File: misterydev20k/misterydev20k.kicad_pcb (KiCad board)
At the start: 2 copper layers, 90 x 67 mm, 178 parts, among them J1 SWD, J11 Joystick 0, J12 Joystick 1, J13 USB_A_Stacked, J2 USB_C_Receptacle_USB2.0, J3 Jumper block, J4 Micro_SD_Card_Det1, J5 HDMI_A, J6 Grove 1125S-4P, J7 USB_A_Stacked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

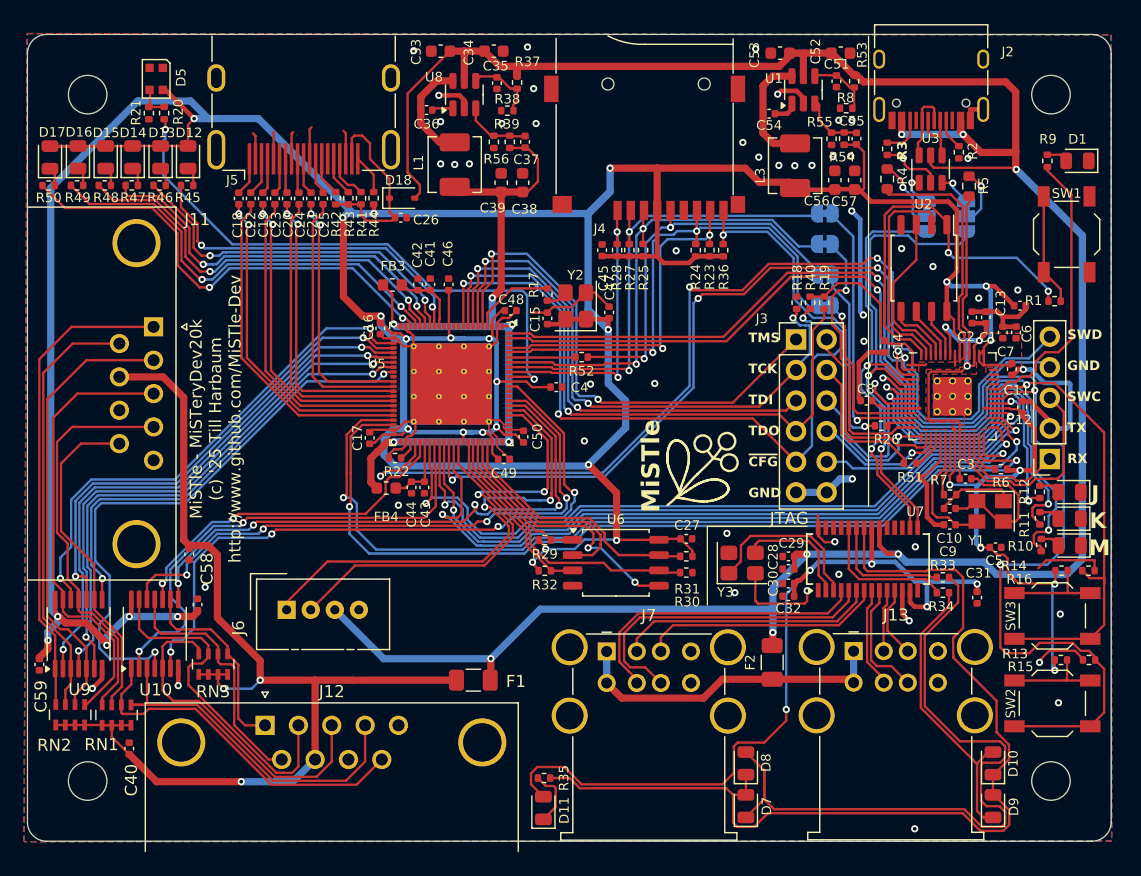
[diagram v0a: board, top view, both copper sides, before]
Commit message: Length match TMDS signals
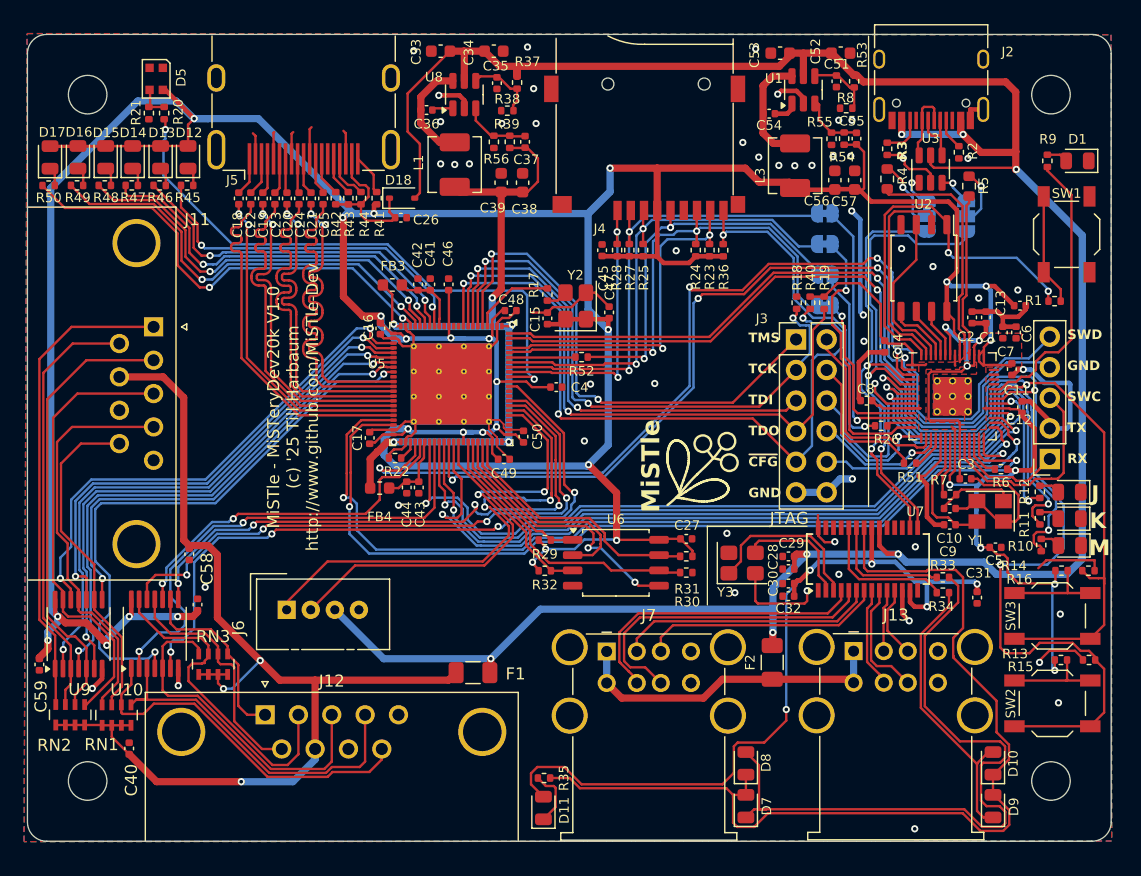
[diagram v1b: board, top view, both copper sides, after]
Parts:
- moved J12 0.87 mm to (119.7, 96.5)
- moved F1 0.63 mm to (137.0, 93.0)
- moved FB4 0.54 mm to (129.2, 77.7)
- moved C43 0.46 mm to (132.5, 77.6)
- moved C44 0.40 mm to (131.5, 77.6)
- moved R41 0.25 mm to (129.0, 53.6)
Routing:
- net +3V3: track 441.4 -> 432.4 mm
- net CK-: track 21.7 -> 29.9 mm
- net CK+: track 20.8 -> 26.9 mm
- net D0-: track 24.2 -> 30.0 mm
- net D1-: track 26.0 -> 30.1 mm
- net 5V_DVI: track 16.8 -> 12.8 mm
- net D0+: track 23.8 -> 27.0 mm
- net D2-: track 27.7 -> 30.2 mm
- net Net-(D7-K): track 60.0 -> 58.1 mm
- net D1+: track 25.4 -> 27.1 mm
- net Net-(RN3-R3.1): track 29.0 -> 27.9 mm
- net MODE0: track 113.6 -> 112.6 mm
- net Net-(RN3-R2.1): track 21.0 -> 20.0 mm
- net Net-(RN3-R1.1): track 16.4 -> 15.4 mm
- net Net-(RN1-R2.1): track 29.4 -> 30.0 mm
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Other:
- board text added: "MiSTle - MiSTeryDev20k V1.0 (c) '25 Till Harbaum http://www.github.com/MiSTle-Dev"
- board text removed: "MiSTle - MiSTeryDev20k (c) '25 Till Harbaum http://www.github.com/MiSTle-Dev"

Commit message: Dev20k LCSC part mapping
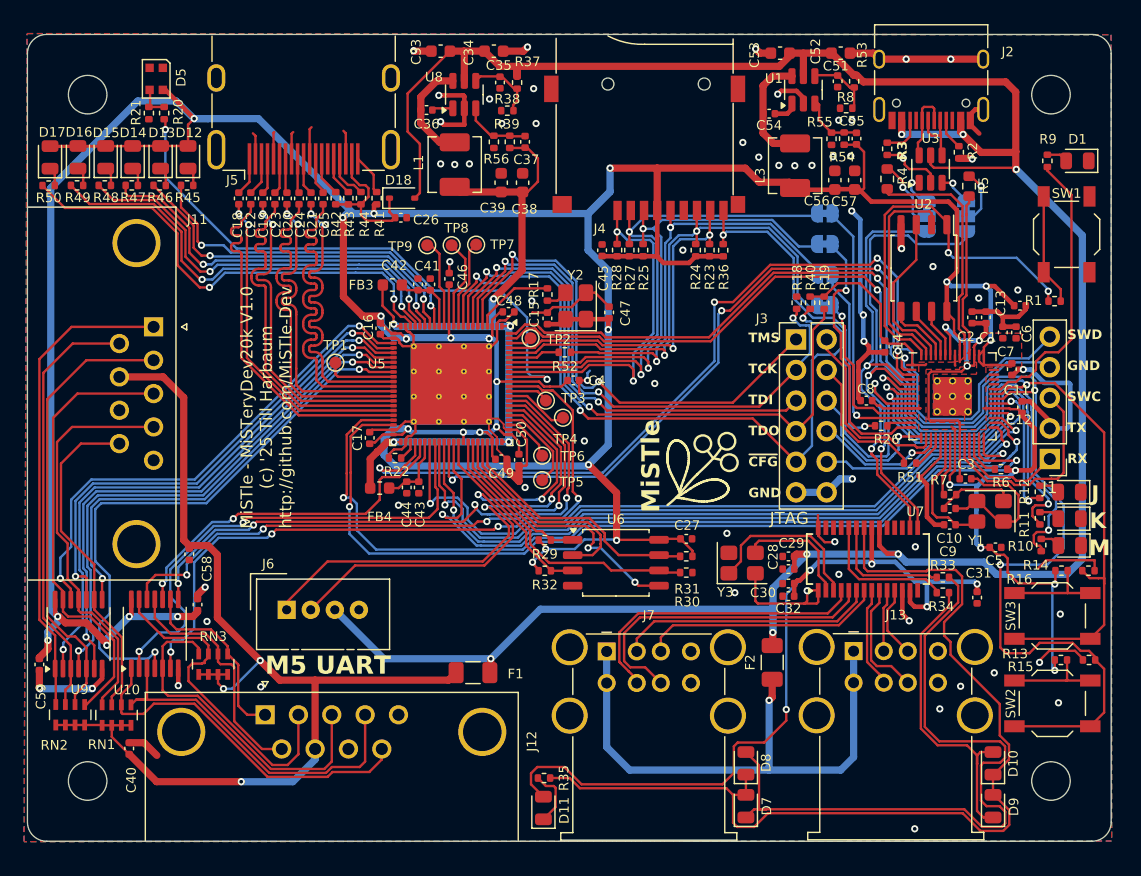
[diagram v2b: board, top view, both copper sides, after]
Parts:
- added TP1: TestPoint, TestPoint:TestPoint_Pad_D1.0mm, F.Cu at (125.6, 67.3)
- added TP2: TestPoint, TestPoint:TestPoint_Pad_D1.0mm, F.Cu at (141.8, 65.2)
- added TP3: TestPoint, TestPoint:TestPoint_Pad_D1.0mm, F.Cu at (143.1, 70.4)
- added TP4: TestPoint, TestPoint:TestPoint_Pad_D1.0mm, F.Cu at (144.5, 71.8)
- added TP5: TestPoint, TestPoint:TestPoint_Pad_D1.0mm, F.Cu at (142.7, 77.0)
- added TP6: TestPoint, TestPoint:TestPoint_Pad_D1.0mm, F.Cu at (142.7, 75.0)
- added TP7: TestPoint, TestPoint:TestPoint_Pad_D1.0mm, F.Cu at (137.3, 57.5)
- added TP8: TestPoint, TestPoint:TestPoint_Pad_D1.0mm, F.Cu at (135.2, 57.5)
- added TP9: TestPoint, TestPoint:TestPoint_Pad_D1.0mm, F.Cu at (133.2, 57.5)
- C41, C43: value 4u7 -> 10uF
- J1: footprint Connector_PinSocket_2.54mm:PinSocket_1x05_P2.54mm_Vertical -> Connector_PinHeader_2.54mm:PinHeader_1x05_P2.54mm_Vertical
- R21: value 5k1 -> 10k
- RN1, RN2, RN3: value R_Pack04 -> 10k
- moved C50 1.97 mm to (140.8, 75.3), turned to 90 degrees
- moved C4 1.53 mm to (145.3, 68.7)
- moved R52 1.45 mm to (144.6, 66.4)
- moved C46 0.46 mm to (135.0, 60.3)
- moved C35 0.26 mm to (139.2, 44.0)
- moved C49 0.22 mm to (139.3, 75.3)
- moved C48 0.20 mm to (140.0, 63.0)
- moved C51 0.10 mm to (167.3, 43.9)
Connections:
- U5 pad 10: unconnected-(U5-IOL29A/GCLKT_6-Pad10) -> Net-(U5-IOL29A/GCLKT_6)
- U5 pad 11: unconnected-(U5-IOL29B/GCLKC_6-Pad11) -> Net-(U5-IOL29B/GCLKC_6)
- U5 pad 13: unconnected-(U5-IOL45A/LPLL2_T_in-Pad13) -> Net-(U5-IOL45A/LPLL2_T_in)
- U5 pad 32: unconnected-(U5-IOB18B-Pad32) -> Net-(U5-IOB18B)
- U5 pad 69: unconnected-(U5-IOT50A-Pad69) -> Net-(U5-IOT50A)
- U5 pad 70: unconnected-(U5-IOT44B-Pad70) -> Net-(U5-IOT44B)
- U5 pad 75: unconnected-(U5-IOT34A-Pad75) -> Net-(U5-IOT34A)
- U5 pad 76: unconnected-(U5-IOT30B/GCLKC_1-Pad76) -> Net-(U5-IOT30B/GCLKC_1)
- U5 pad 86: unconnected-(U5-IOT4A-Pad86) -> Net-(U5-IOT4A)
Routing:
- net GND: track 186.4 -> 249.7 mm, vias 51 -> 63
- net Net-(J13-VBUS1): track 27.0 -> 46.5 mm, vias 0 -> 1
- net Net-(U5-IOL29B/GCLKC_6): track 0.00 -> 7.59 mm
- net Net-(U5-IOT44B): track 0.00 -> 7.49 mm
- net Net-(U5-IOL45A/LPLL2_T_in): track 0.00 -> 7.48 mm
- net Net-(U5-IOL29A/GCLKT_6): track 0.00 -> 7.38 mm
- net Net-(U5-IOB18B): track 0.00 -> 5.87 mm
- net SD_DAT2: track 24.3 -> 30.1 mm
- net Net-(U5-IOT34A): track 0.00 -> 5.39 mm
- net SD_DAT3: track 40.7 -> 45.5 mm
- net Net-(U5-IOT50A): track 0.00 -> 4.18 mm
- net Net-(U5-IOT30B/GCLKC_1): track 0.00 -> 3.43 mm
- net SD_CMD: track 40.8 -> 43.3 mm
- net DBG RX: track 91.8 -> 89.6 mm
- net /GW2AR-LV18 FPGA/Interfaces/SD_CLK: track 32.7 -> 34.9 mm
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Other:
- board text added: "M5 UART"
- board text added: "MiSTle - MiSTeryDev20k V1.0 (c) '25 Till Harbaum http://github.com/MiSTle-Dev"
- board text removed: "MiSTle - MiSTeryDev20k V1.0 (c) '25 Till Harbaum http://www.github.com/MiSTle-Dev"

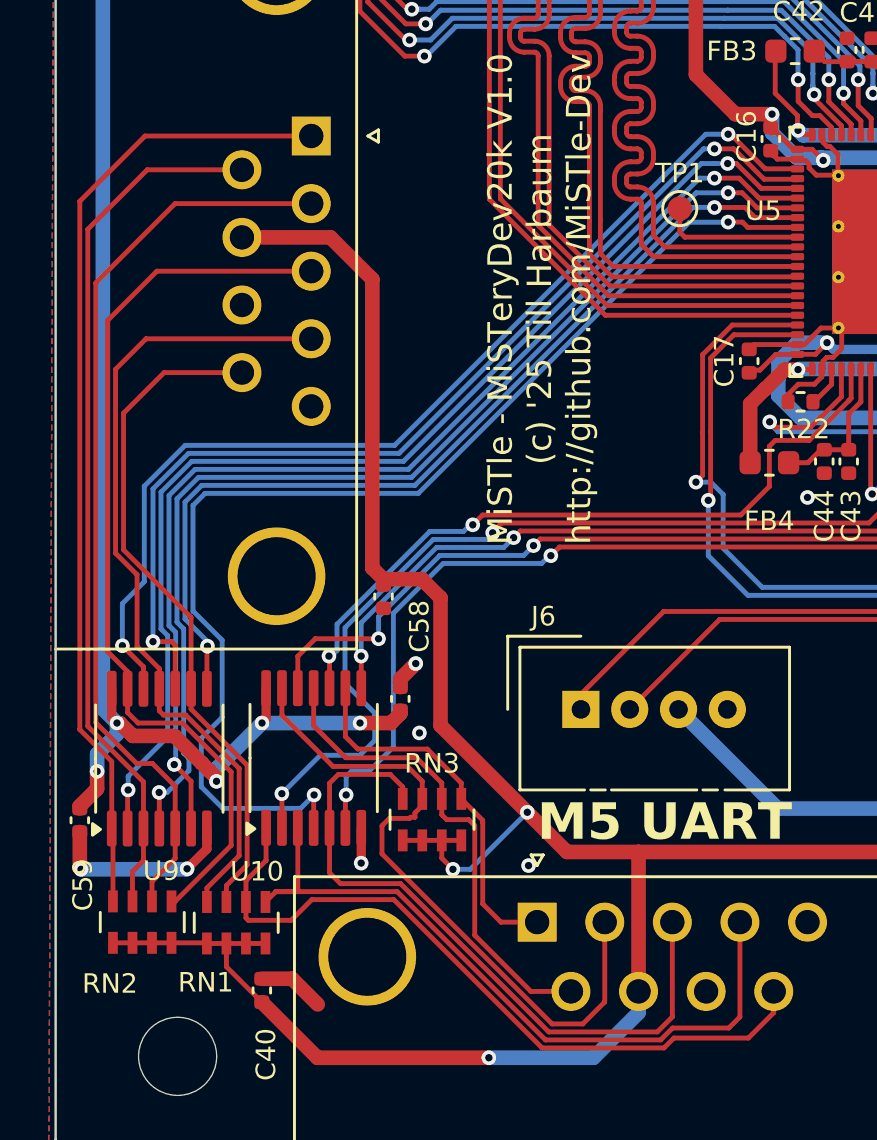
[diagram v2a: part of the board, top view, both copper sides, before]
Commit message: Fix joystick connections
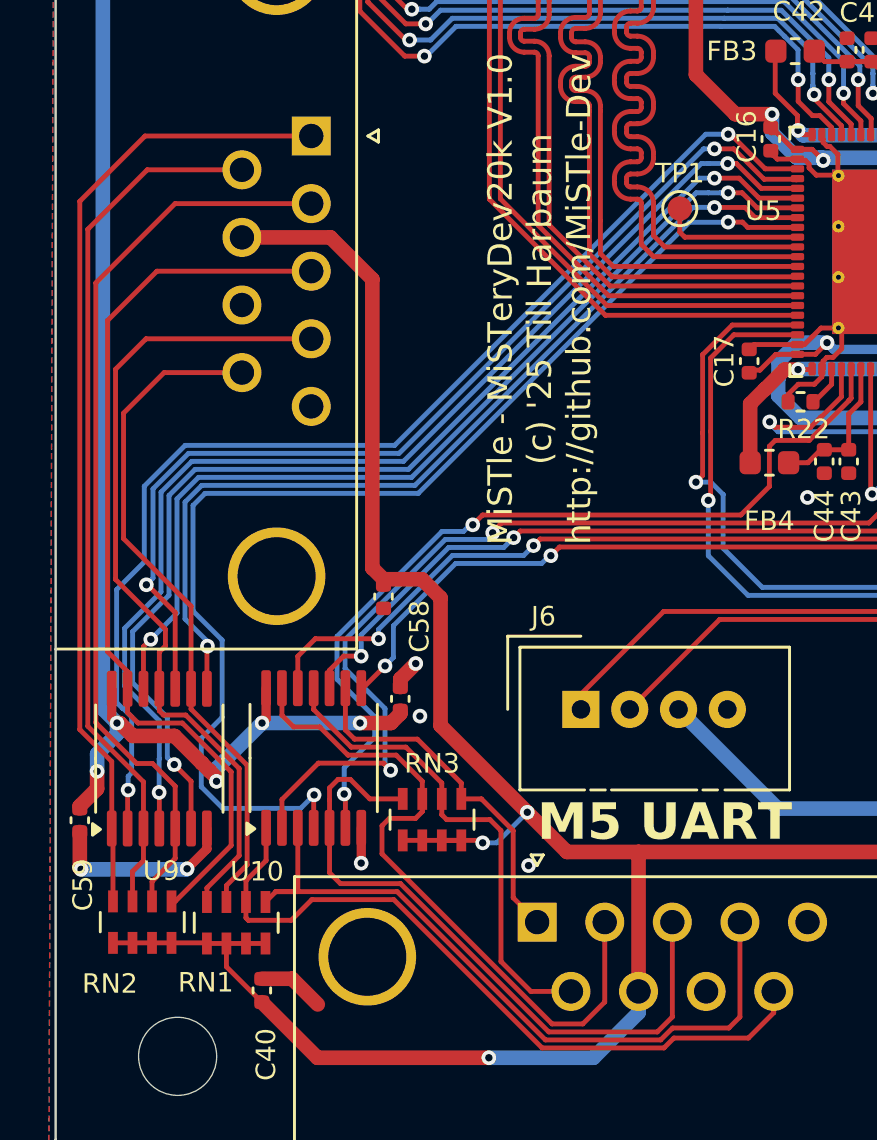
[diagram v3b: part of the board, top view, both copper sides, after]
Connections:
- U10 pad 10: JOYB4 -> JOYB0
- U10 pad 6: JOYB2 -> JOYB4
- U10 pad 8: JOYB0 -> JOYB2
- U9 pad 12: JOYA2 -> JOYA4
- U9 pad 2: JOYA0 -> JOYA2
- U9 pad 4: JOYA4 -> JOYA0
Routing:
- net JOYB2: track 57.9 -> 51.3 mm
- net JOYB4: track 29.9 -> 36.3 mm
- net JOYA2: track 42.4 -> 48.2 mm
- net JOYA4: track 45.3 -> 39.5 mm
- net JOYB5: track 41.3 -> 42.7 mm
- net Net-(RN1-R1.2): track 89.7 -> 88.3 mm
- net JOYA1: track 45.5 -> 46.7 mm
- net JOYB0: track 48.8 -> 49.5 mm
- net Net-(RN3-R4.1): track 28.4 -> 27.8 mm
- net Net-(RN3-R1.1): track 15.4 -> 14.8 mm

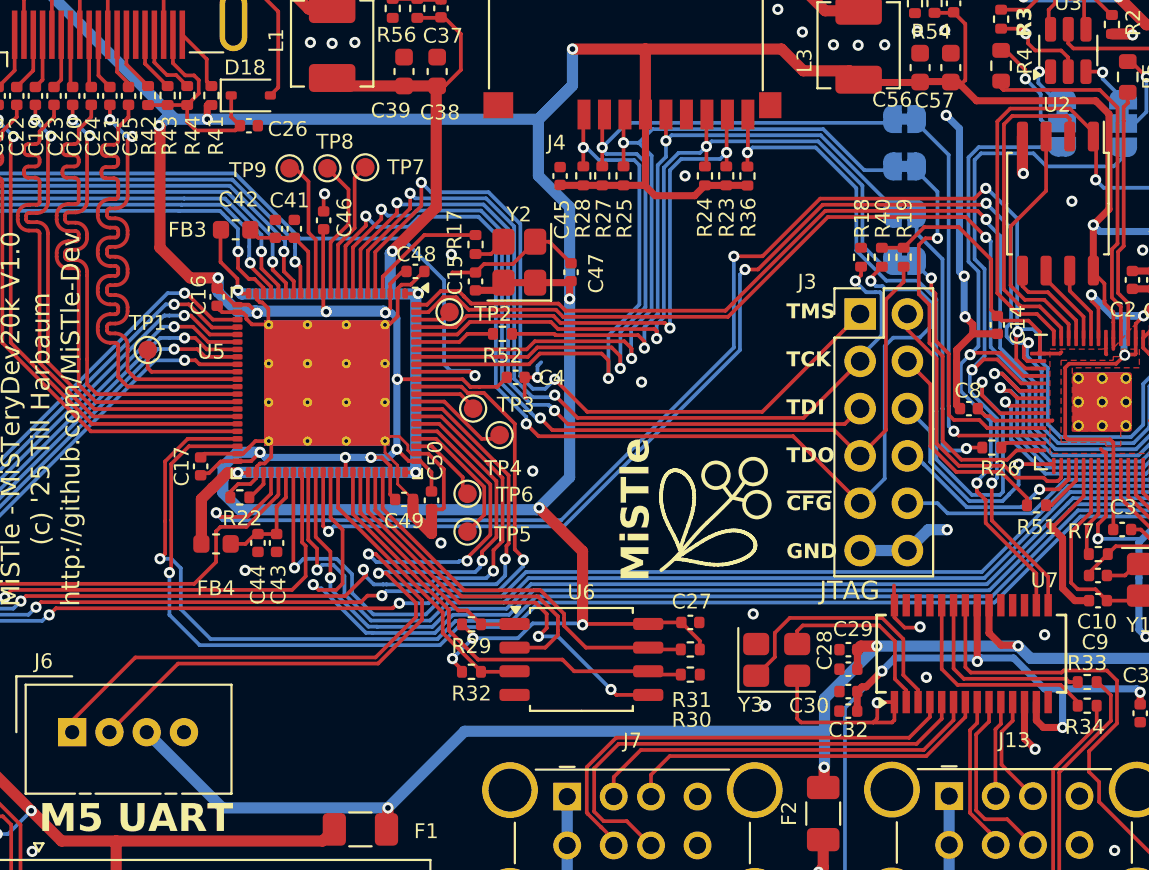
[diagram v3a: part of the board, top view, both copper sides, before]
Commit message: Update debug UART wiring
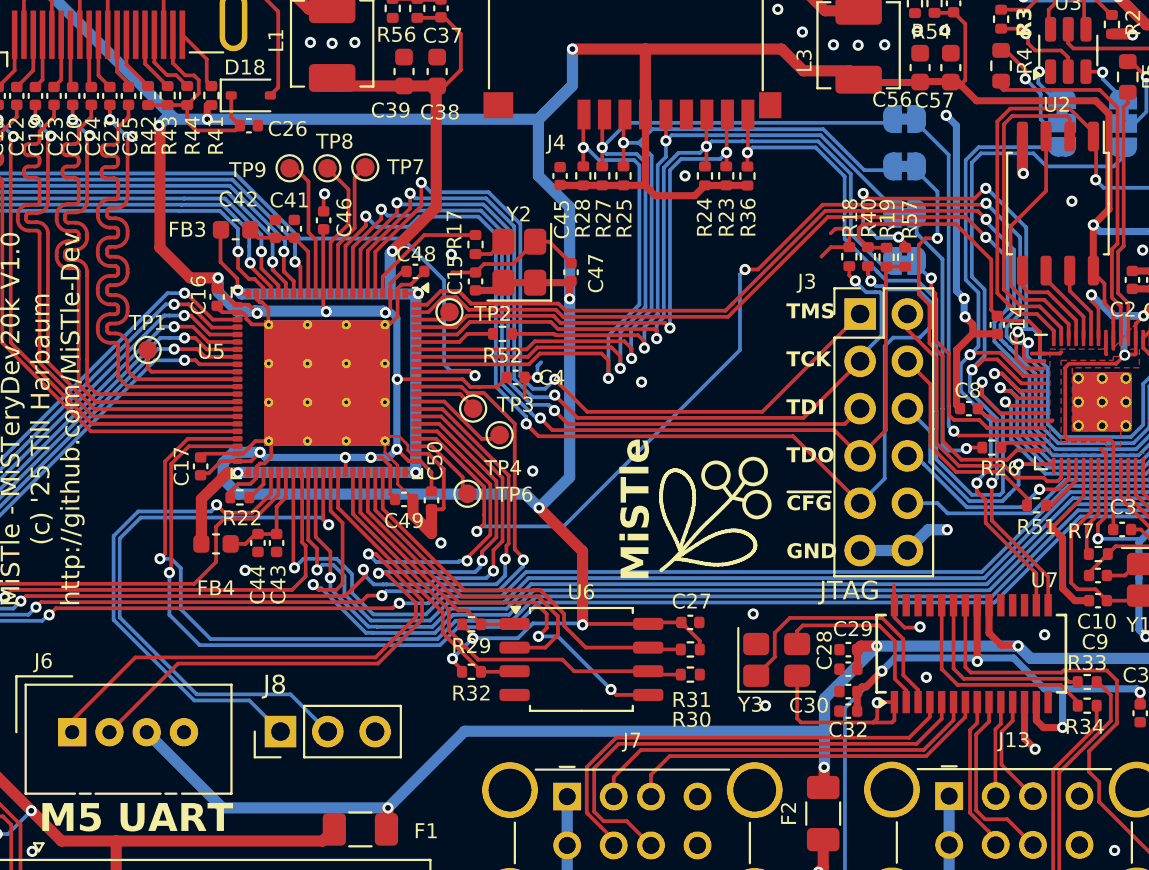
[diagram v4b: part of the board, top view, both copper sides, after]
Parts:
- removed TP5: TestPoint, TestPoint:TestPoint_Pad_D1.0mm
- added J8: EXT UART, Connector_PinHeader_2.54mm:PinHeader_1x03_P2.54mm_Vertical, F.Cu at (132.7, 87.8)
- added R57: 560, Resistor_SMD:R_0402_1005Metric, F.Cu at (166.2, 62.3)
- moved R19 0.92 mm to (165.2, 62.3)
- moved R40 0.75 mm to (164.2, 62.2)
- moved R18 0.63 mm to (163.2, 62.2)
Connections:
- net Net-(J3-Pin_7) renamed /GW2AR-LV18 FPGA/UART_TX
- net UART_RX renamed MIDI_IN
- net UART_TX renamed MIDI_OUT
- U5 pad 48: DBG RX -> MON_TX
- U5 pad 55: DBG TX -> MON_RX
- U5 pad 70: Net-(U5-IOT44B) -> DBG TX
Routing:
- net DBG RX: track 89.6 -> 45.2 mm
- net MON_RX: track 0.00 -> 32.7 mm, vias 0 -> 1
- net MON_TX: track 0.00 -> 26.9 mm, vias 0 -> 1
- net Net-(U5-IOT44B): track 7.49 -> 0.00 mm
- net GND: track 249.7 -> 253.5 mm
- net DBG TX: track 80.0 -> 76.4 mm
- net +3V3: track 434.3 -> 437.0 mm
- net /GW2AR-LV18 FPGA/UART_TX: track 52.7 -> 53.4 mm
- net MODE0: track 113.2 -> 113.8 mm
- net MODE1: track 97.0 -> 97.6 mm
